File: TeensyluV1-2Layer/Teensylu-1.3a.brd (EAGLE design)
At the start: 101.6 x 76.2 mm, 110 parts, among them J1 22ga, J10 MICROSD, J11 USB-MICRO-PTH, J12 M02POLAR, J13 4P-TERM-BLOCK284391-4, J14 HOTEND-1, J15 39-29-3066, J16 2x7, J17 HOTBED, J18 M02POLAR, J19 M02POLAR, J2 22ga, J3 22ga, J4 22ga, J5 22ga, J6 22ga, J7 22ga, J8 M02POLAR, J9 M02POLAR, P1 POLOLU-X, P2 POLOLU-Y, P3 POLOLU-Z, P4 POLOLU-E1, Q1 PMV45EN, Q2 PSMN1R2-30YLC, Q3 MMUN2211LT3G, Q4 PSMN1R2-30YLC, U1 LMR16006X, U2 DRTR5V0U2SR, U3 AP7313SOT23C, U4 TXB0104TSSOP14, U5 AT90USB1286, X1 16MHZ

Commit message: Updated heater mosfets
I updated the heater mosfets to 40v version, part # PSMN1R8-40YLC,115
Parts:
- Q2, Q4: value PSMN1R2-30YLC -> PSMN1R8-40YLC
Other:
- board text added: "Rev. 1.3a"
- board text removed: "Rev. 1.3"
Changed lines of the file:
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@@
 <text x="49.276" y="10.922" size="0.8128" layer="121" font="vector" ratio="15" rot="R180">+12V</text>
 <text x="62.738" y="30.48" size="1.27" layer="121" font="vector" ratio="15">TeensyluV1 2Layer</text>
-<text x="62.738" y="28.702" size="1.27" layer="121" font="vector" ratio="15">Rev. 1.3</text>
+<text x="62.738" y="28.702" size="1.27" layer="121" font="vector" ratio="15">Rev. 1.3a</text>
 <text x="62.738" y="27.178" size="1.016" layer="121" font="vector" ratio="15">https://github.com/StephS/Teensylu</text>
 <text x="62.738" y="25.654" size="1.016" layer="121" font="vector" ratio="15">Licensed CC-BY-SA</text>
@@
 <attribute name="VDC" value="16V" x="32.766" y="20.574" size="1.778" layer="27" rot="R315" display="off"/>
 </element>
-<element name="Q2" library="teensylu" package="LFPACK-POWERPAK-SO8" value="PSMN1R2-30YLC" x="13.208" y="44.958" smashed="yes" rot="R90">
+<element name="Q2" library="teensylu" package="LFPACK-POWERPAK-SO8" value="PSMN1R8-40YLC" x="13.208" y="44.958" smashed="yes" rot="R90">
 <attribute name="CURRENT" value="100A" x="13.208" y="44.958" size="1.778" layer="27" rot="R90" display="off"/>
 <attribute name="MANUFACTURER" value="NXP Semiconductors" x="13.208" y="44.958" size="1.778" layer="27" rot="R90" display="off"/>
-<attribute name="VOLTAGE" value="30V" x="13.208" y="44.958" size="1.778" layer="27" rot="R90" display="off"/>
+<attribute name="VOLTAGE" value="40V" x="13.208" y="44.958" size="1.778" layer="27" rot="R90" display="off"/>
 <attribute name="VGS" value="1.95V" x="13.208" y="44.958" size="1.778" layer="27" rot="R90" display="off"/>
-<attribute name="MANUFACTURER_PART_NUMBER" value="PSMN1R2-30YLC,115" x="13.208" y="44.958" size="1.778" layer="27" rot="R90" display="off"/>
-<attribute name="RDS_ON" value="1.25mOhm" x="13.208" y="44.958" size="1.778" layer="27" rot="R90" display="off"/>
+<attribute name="MANUFACTURER_PART_NUMBER" value="PSMN1R8-40YLC,115" x="13.208" y="44.958" size="1.778" layer="27" rot="R90" display="off"/>
+<attribute name="RDS_ON" value="1.8mOhm" x="13.208" y="44.958" size="1.778" layer="27" rot="R90" display="off"/>
 <attribute name="NAME" x="17.018" y="41.9735" size="1.016" layer="121" ratio="18" rot="R180"/>
 </element>
-<element name="Q4" library="teensylu" package="LFPACK-POWERPAK-SO8" value="PSMN1R2-30YLC" x="13.208" y="29.718" smashed="yes" rot="R90">
+<element name="Q4" library="teensylu" package="LFPACK-POWERPAK-SO8" value="PSMN1R8-40YLC" x="13.208" y="29.718" smashed="yes" rot="R90">
 <attribute name="CURRENT" value="100A" x="13.208" y="29.718" size="1.778" layer="27" rot="R90" display="off"/>
 <attribute name="MANUFACTURER" value="NXP Semiconductors" x="13.208" y="29.718" size="1.778" layer="27" rot="R90" display="off"/>
-<attribute name="VOLTAGE" value="30V" x="13.208" y="29.718" size="1.778" layer="27" rot="R90" display="off"/>
+<attribute name="VOLTAGE" value="40V" x="13.208" y="29.718" size="1.778" layer="27" rot="R90" display="off"/>
 <attribute name="VGS" value="1.95V" x="13.208" y="29.718" size="1.778" layer="27" rot="R90" display="off"/>
-<attribute name="MANUFACTURER_PART_NUMBER" value="PSMN1R2-30YLC,115" x="13.208" y="29.718" size="1.778" layer="27" rot="R90" display="off"/>
-<attribute name="RDS_ON" value="1.25mOhm" x="13.208" y="29.718" size="1.778" layer="27" rot="R90" display="off"/>
+<attribute name="MANUFACTURER_PART_NUMBER" value="PSMN1R8-40YLC,115" x="13.208" y="29.718" size="1.778" layer="27" rot="R90" display="off"/>
+<attribute name="RDS_ON" value="1.8mOhm" x="13.208" y="29.718" size="1.778" layer="27" rot="R90" display="off"/>
 <attribute name="NAME" x="17.2085" y="30.988" size="1.016" layer="121" ratio="18" rot="R270"/>
 </element>

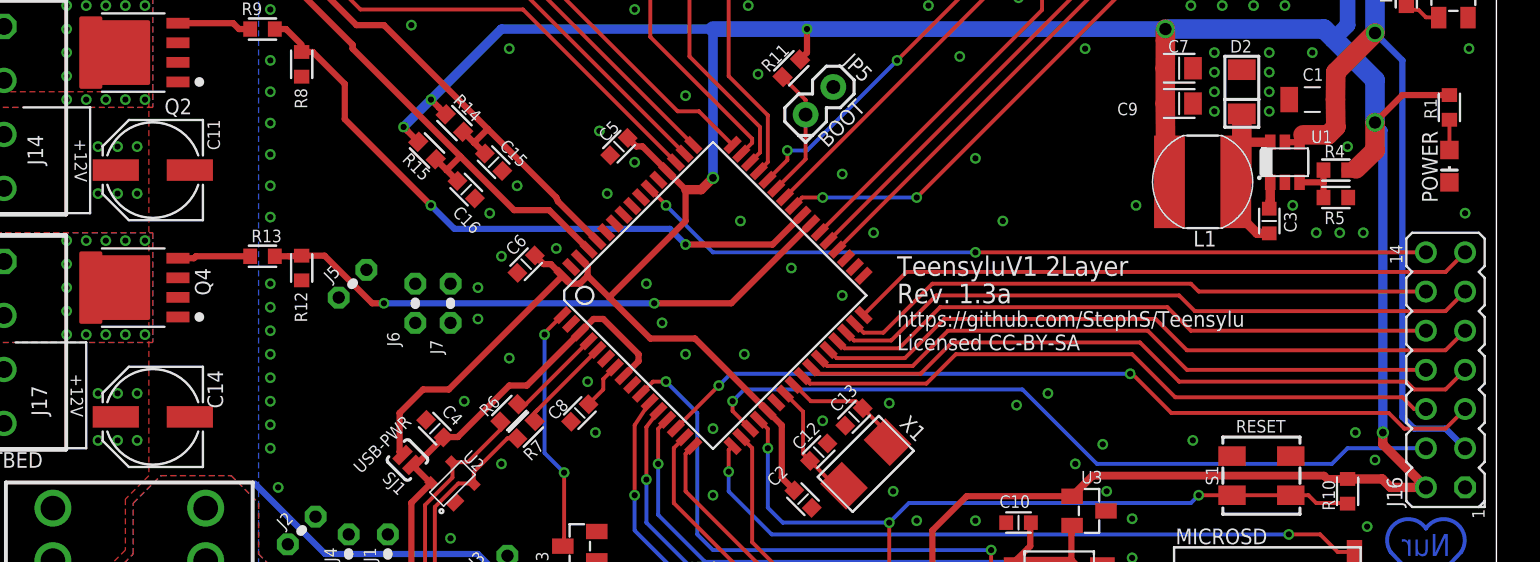
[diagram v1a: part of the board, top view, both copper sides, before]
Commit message: minor routing changes
just a few changes to clean up routing.
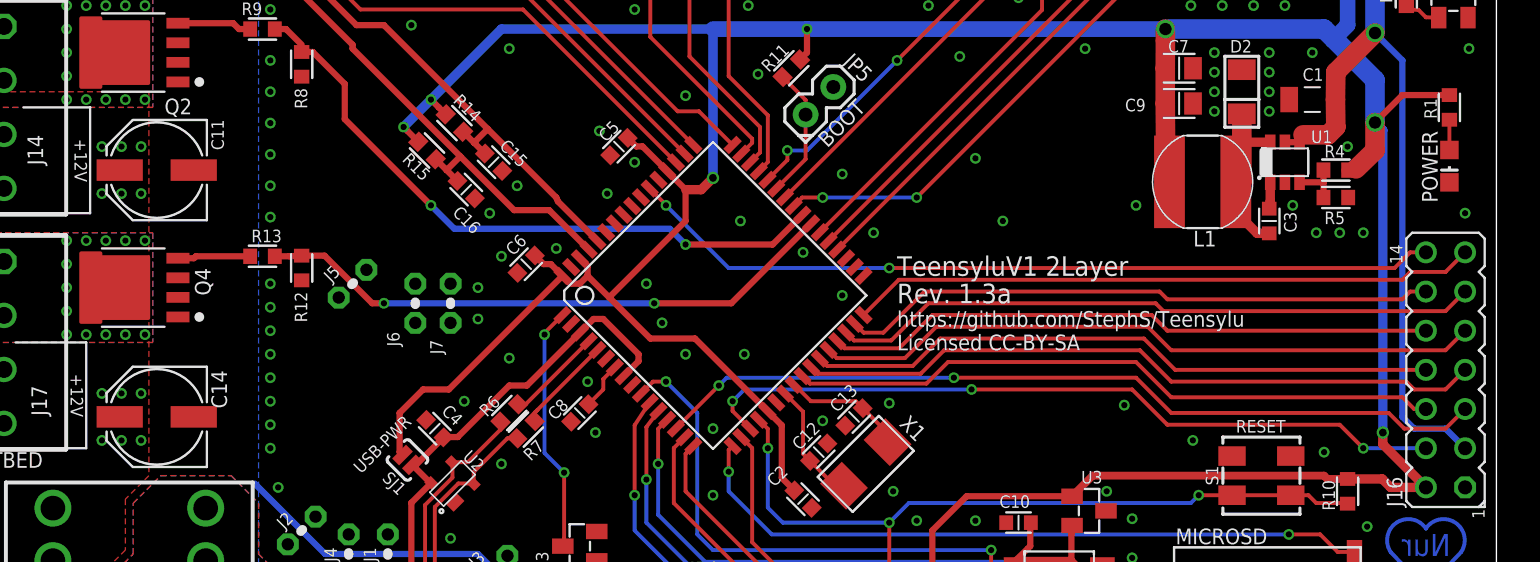
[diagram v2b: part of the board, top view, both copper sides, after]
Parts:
- moved C11 0.25 mm to (14.7, 37.3)
- moved C14 0.25 mm to (14.7, 21.3)
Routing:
- net PE5: track 49.9 -> 49.1 mm, vias 1 -> 3
- net A7: track 52.1 -> 52.9 mm

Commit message: Added dimensions
Dimensions are added to make it easier to make enclosures.
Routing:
- net PE5: vias 3 -> 2
- net 5V: vias 12 -> 11
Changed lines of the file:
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@@
 <layer number="116" name="drillImage" color="9" fill="1" visible="yes" active="yes"/>
 <layer number="121" name="_tsilk" color="13" fill="1" visible="yes" active="yes"/>
-<layer number="122" name="_bsilk" color="11" fill="1" visible="no" active="yes"/>
+<layer number="122" name="_bsilk" color="11" fill="1" visible="yes" active="yes"/>
 <layer number="125" name="_tNames" color="7" fill="1" visible="yes" active="yes"/>
 <layer number="144" name="Drill_legend" color="7" fill="1" visible="yes" active="yes"/>
@@
 <wire x1="50.8" y1="68.834" x2="50.8" y2="70.104" width="0.1524" layer="121"/>
 <wire x1="47.498" y1="70.104" x2="48.26" y2="70.104" width="0.1524" layer="121"/>
+<dimension x1="3.81" y1="0" x2="3.81" y2="3.81" x3="-3.048" y3="1.905" textsize="1.778" layer="51" unit="inch"/>
+<dimension x1="3.81" y1="0" x2="3.81" y2="72.39" x3="-7.366" y3="36.195" textsize="1.778" layer="51" unit="inch"/>
+<dimension x1="3.81" y1="0" x2="3.81" y2="76.2" x3="-11.176" y3="38.1" textsize="1.778" layer="51" unit="inch"/>
+<dimension x1="0" y1="3.81" x2="3.81" y2="3.81" x3="1.905" y3="-6.096" textsize="1.778" layer="51" unit="inch"/>
+<dimension x1="0" y1="3.81" x2="97.79" y2="3.81" x3="48.895" y3="-14.986" textsize="1.778" layer="51" unit="inch"/>
+<dimension x1="0" y1="3.81" x2="101.6" y2="3.81" x3="50.8" y3="-18.288" textsize="1.778" layer="51" unit="inch"/>
+<dimension x1="0" y1="3.81" x2="80.772" y2="3.81" x3="40.386" y3="-8.89" textsize="1.778" layer="51" unit="inch"/>
+<dimension x1="80.772" y1="3.81" x2="92.71" y2="3.81" x3="86.741" y3="-8.89" textsize="1.778" layer="51" unit="inch"/>
 </plain>
 <attributes>
@@
 <wire x1="48.006" y1="8.636" x2="39.37" y2="8.636" width="0.4064" layer="16"/>
 <wire x1="39.37" y1="8.636" x2="35.56" y2="12.446" width="0.4064" layer="16"/>
-<wire x1="37.338" y1="3.302" x2="37.338" y2="6.604" width="0.4064" layer="16"/>
-<wire x1="37.338" y1="6.604" x2="39.37" y2="8.636" width="0.4064" layer="16"/>
+<wire x1="37.338" y1="3.302" x2="37.338" y2="6.096" width="0.4064" layer="16"/>
+<wire x1="37.338" y1="6.096" x2="39.37" y2="8.128" width="0.4064" layer="16"/>
+<wire x1="39.37" y1="8.128" x2="39.37" y2="8.636" width="0.4064" layer="16"/>
 <contactref element="C11" pad="+"/>
 <via x="11.176" y="35.814" extent="1-16" drill="0.4"/>
@@
 <wire x1="67.564" y1="23.114" x2="77.978" y2="23.114" width="0.254" layer="1"/>
 <wire x1="77.978" y1="23.114" x2="80.264" y2="20.828" width="0.254" layer="1"/>
-<wire x1="80.264" y1="20.828" x2="91.44" y2="20.828" width="0.254" layer="1"/>
-<wire x1="91.44" y1="20.828" x2="92.964" y2="19.304" width="0.254" layer="1"/>
-<wire x1="92.964" y1="19.304" x2="97.028" y2="19.304" width="0.254" layer="16"/>
+<wire x1="80.264" y1="20.828" x2="93.98" y2="20.828" width="0.254" layer="1"/>
+<wire x1="93.98" y1="20.828" x2="95.504" y2="19.304" width="0.254" layer="1"/>
+<wire x1="95.504" y1="19.304" x2="97.028" y2="19.304" width="0.254" layer="1"/>
 <wire x1="53.2041625" y1="20.583296875" x2="52.07" y2="21.717459375" width="0.254" layer="1"/>
 <wire x1="52.07" y1="21.717459375" x2="52.07" y2="22.352" width="0.254" layer="1"/>
@@
 <wire x1="52.07" y1="22.352" x2="52.832" y2="23.114" width="0.254" layer="16"/>
 <wire x1="52.832" y1="23.114" x2="67.564" y2="23.114" width="0.254" layer="16"/>
-<via x="92.964" y="19.304" extent="1-16" drill="0.4"/>
 <via x="67.564" y="23.114" extent="1-16" drill="0.4"/>
 </signal>
@@
 <wire x1="98.552" y1="42.202" x2="95.504" y2="42.202" width="0.4064" layer="1"/>
 <wire x1="95.504" y1="42.202" x2="93.726" y2="40.424" width="0.4064" layer="1"/>
-<wire x1="97.028" y1="16.764" x2="94.234" y2="19.558" width="0.6096" layer="1"/>
-<wire x1="94.234" y1="19.558" x2="94.234" y2="20.32" width="0.6096" layer="1"/>
-<via x="94.234" y="20.32" extent="1-16" drill="0.5"/>
-<wire x1="94.234" y1="20.32" x2="94.234" y2="39.916" width="0.6096" layer="16"/>
+<wire x1="97.028" y1="16.764" x2="94.234" y2="19.558" width="0.6096" layer="16"/>
+<wire x1="94.234" y1="19.558" x2="94.234" y2="39.916" width="0.6096" layer="16"/>
 <wire x1="94.234" y1="39.916" x2="93.726" y2="40.424" width="0.6096" layer="16"/>
 <wire x1="91.948" y1="17.31" x2="94.196" y2="17.31" width="0.6096" layer="1"/>
